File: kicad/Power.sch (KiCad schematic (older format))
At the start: 10 parts

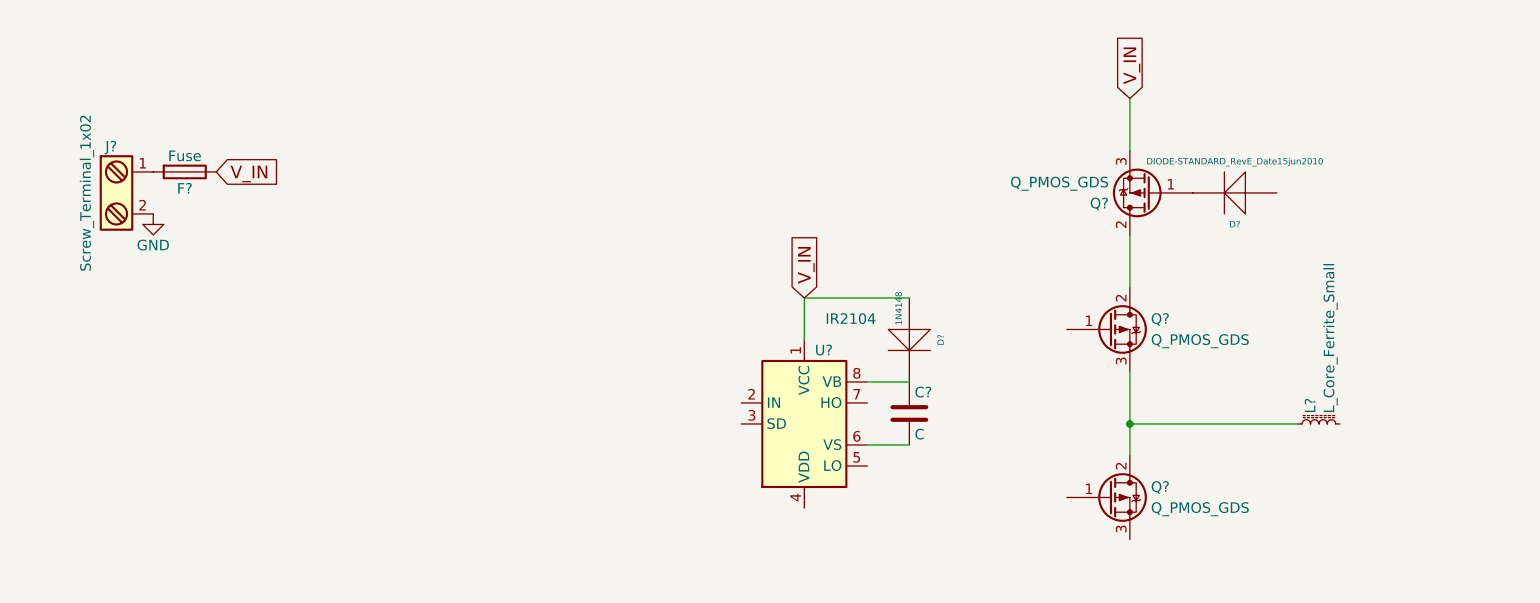
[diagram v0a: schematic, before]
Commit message: Schematical hierarchical structure enhanced
Work on schematical page KiCad
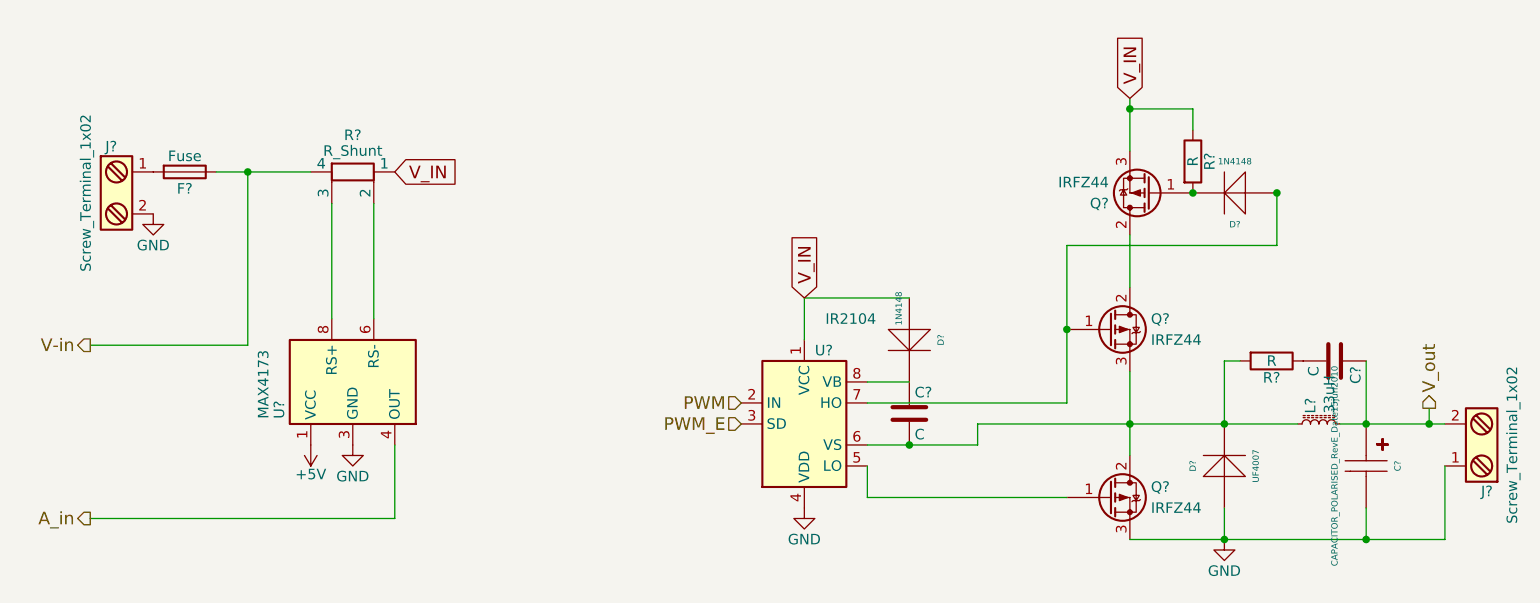
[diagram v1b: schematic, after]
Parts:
- added C?: C, symbol C
- added C?: CAPACITOR_POLARISED_RevE_Date15jun2010, symbol CAPACITOR_POLARISED_RevE_Date15jun2010
- added D?: UF4007, symbol DIODE-STANDARD_RevE_Date15jun2010
- added J?: Screw_Terminal_1x02, symbol Screw_Terminal_1x02
- added R?: R_Shunt, symbol R_Shunt
- added R? (x2): R, symbol R
- added U?: MAX4173, SOIC-8, symbol MAX4173
- D?: value DIODE-STANDARD_RevE_Date15jun2010 -> 1N4148
- L?: value L_Core_Ferrite_Small -> 33uH
- Q? (x3): value Q_PMOS_GDS -> IRFZ44
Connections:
- net GND: now also Q?.3 (S), U?.4 (VDD), C?.2, D?.1 (A), J?.1, U?.3 (GND)
- net V_IN: now also R?.1, R?.1; no longer F?.1
- net at D?.2 (K), Q?.1 (G): now also R?.2
- net at Q?.1 (G): now also D?.1 (A), U?.7 (HO)
- net at L?.1, Q?.2 (D), Q?.3 (S): now also C?.2, U?.6 (VS), D?.2 (K), R?.2
- net at Q?.1 (G): now also U?.5 (LO)
- net PWM: now reaches U?.2 (IN)
- net PWM_E: now reaches U?.3 (SD)
- net V_out: now reaches L?.2
- net V_out: now also C?.1, C?.1, J?.2
- new net: R?.2, U?.6 (RS-)
- new net: R?.3, U?.8 (RS+)
- new net: C?.2, R?.1
- new net +5V: U?.1 (VCC)
- new net A_in: U?.4 (OUT)
- new net V-in: F?.1, R?.4
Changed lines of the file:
@@
 	1    0    0    -1
 $EndComp
-Text GLabel 2150 2050 2    60   Input ~ 0
+Text GLabel 3000 2050 2    60   Input ~ 0
 V_IN
 $Comp
@@
 P 6600 2150
 F 0 "Q?" H 6800 2200 50  0000 L CNN
-F 1 "Q_PMOS_GDS" H 6800 2100 50  0000 L CNN
+F 1 "IRFZ44" H 6800 2100 50  0000 L CNN
 F 2 "" H 6800 2250 50  0001 C CNN
 F 3 "" H 6600 2150 50  0001 C CNN
@@
 P 6400 2800
 F 0 "Q?" H 6600 2850 50  0000 L CNN
-F 1 "Q_PMOS_GDS" H 6600 2750 50  0000 L CNN
+F 1 "IRFZ44" H 6600 2750 50  0000 L CNN
 F 2 "" H 6600 2900 50  0001 C CNN
 F 3 "" H 6400 2800 50  0001 C CNN
@@
 P 6400 3600
 F 0 "Q?" H 6600 3650 50  0000 L CNN
-F 1 "Q_PMOS_GDS" H 6600 3550 50  0000 L CNN
+F 1 "IRFZ44" H 6600 3550 50  0000 L CNN
 F 2 "" H 6600 3700 50  0001 C CNN
 F 3 "" H 6400 3600 50  0001 C CNN
@@
 P 7000 2150
 F 0 "D?" H 7000 2300 30  0000 C CNN
-F 1 "DIODE-STANDARD_RevE_Date15jun2010" H 7000 2000 30  0000 C CNN
+F 1 "1N4148" H 7000 2000 30  0000 C CNN
 F 2 "" H 7000 2150 60  0001 C CNN
 F 3 "" H 7000 2150 60  0001 C CNN
@@
 P 7400 3250
 F 0 "L?" H 7450 3290 50  0000 L CNN
-F 1 "L_Core_Ferrite_Small" H 7450 3200 50  0000 L CNN
+F 1 "33uH" H 7450 3200 50  0000 L CNN
 F 2 "" H 7400 3250 50  0001 C CNN
 F 3 "" H 7400 3250 50  0001 C CNN
@@
 $EndComp
 Wire Wire Line
-	6500 1950 6500 1700
+	6500 1700 6500 1950
 Wire Wire Line
 	6500 2600 6500 2350
 Wire Wire Line
-	6500 3400 6500 3000
-Wire Wire Line
-	7300 3250 6500 3250
+	6500 3000 6500 3400
+Wire Wire Line
+	5775 3250 7300 3250
 Connection ~ 6500 3250
 Text GLabel 4950 2650 1    60   Input ~ 0
@@
 $EndComp
 Wire Wire Line
-	5450 3350 5250 3350
+	5250 3350 5775 3350
+$Comp
+L R_Shunt R?
+U 1 1 5B82012D
+P 2800 2050
+F 0 "R?" V 2625 2050 50  0000 C CNN
+F 1 "R_Shunt" V 2700 2050 50  0000 C CNN
+F 2 "" V 2730 2050 50  0001 C CNN
+F 3 "" H 2800 2050 50  0001 C CNN
+	1    2800 2050
+	0    1    1    0
+$EndComp
+Wire Wire Line
+	2150 2050 2600 2050
+$Comp
+L MAX4173 U?
+U 1 1 5B820270
+P 2800 3050
+F 0 "U?" H 2625 3400 50  0000 L CNN
+F 1 "MAX4173" H 2625 3475 50  0000 L CNN
+F 2 "SOIC-8" H 2800 2700 50  0001 C CIN
+F 3 "" H 2800 3050 50  0001 C CNN
+	1    2800 3050
+	0    -1   -1   0
+$EndComp
+Wire Wire Line
+	2700 2750 2700 2200
+Wire Wire Line
+	2900 2750 2900 2200
+Wire Wire Line
+	2300 2050 2300 2875
+Wire Wire Line
+	2300 2875 1550 2875
+Connection ~ 2300 2050
+Text HLabel 1550 2875 0    60   Output ~ 0
+V-in
+Wire Wire Line
+	3000 3700 1550 3700
+Wire Wire Line
+	3000 3350 3000 3700
+Text HLabel 1550 3700 0    60   Output ~ 0
+A_in
+$Comp
+L +5V #PWR?
+U 1 1 5B82066B
+P 2600 3350
+F 0 "#PWR?" H 2600 3200 50  0001 C CNN
+F 1 "+5V" H 2600 3490 50  0000 C CNN
+F 2 "" H 2600 3350 50  0001 C CNN
+F 3 "" H 2600 3350 50  0001 C CNN
+	1    2600 3350
+	-1   0    0    1
+$EndComp
+$Comp
+L GND #PWR?
+U 1 1 5B8206A3
+P 2800 3350
+F 0 "#PWR?" H 2800 3100 50  0001 C CNN
+F 1 "GND" H 2800 3200 50  0000 C CNN
+F 2 "" H 2800 3350 50  0001 C CNN
+F 3 "" H 2800 3350 50  0001 C CNN
+	1    2800 3350
+	1    0    0    -1
+$EndComp
+Text HLabel 4650 3150 0    60   Input ~ 0
+PWM
+Text HLabel 4650 3250 0    60   Input ~ 0
+PWM_E
+Wire Wire Line
+	5775 3350 5775 3250
+Connection ~ 5450 3350
+Wire Wire Line
+	6200 3150 5250 3150
+Wire Wire Line
+	6200 2400 6200 3150
+Wire Wire Line
+	6200 2400 7200 2400
+Wire Wire Line
+	7200 2400 7200 2150
+Connection ~ 6200 2800
+$Comp
+L R R?
+U 1 1 5B83631E
+P 6800 2000
+F 0 "R?" V 6880 2000 50  0000 C CNN
+F 1 "R" V 6800 2000 50  0000 C CNN
+F 2 "" V 6730 2000 50  0001 C CNN
+F 3 "" H 6800 2000 50  0001 C CNN
+	1    6800 2000
+	1    0    0    -1
+$EndComp
+Connection ~ 6800 2150
+Connection ~ 7200 2150
+Wire Wire Line
+	6800 1850 6800 1750
+Wire Wire Line
+	6800 1750 6500 1750
+Connection ~ 6500 1750
+Wire Wire Line
+	6200 3600 5250 3600
+Wire Wire Line
+	5250 3600 5250 3450
+$Comp
+L GND #PWR?
+U 1 1 5B83651E
+P 4950 3650
+F 0 "#PWR?" H 4950 3400 50  0001 C CNN
+F 1 "GND" H 4950 3500 50  0000 C CNN
+F 2 "" H 4950 3650 50  0001 C CNN
+F 3 "" H 4950 3650 50  0001 C CNN
+	1    4950 3650
+	1    0    0    -1
+$EndComp
+$Comp
+L GND #PWR?
+U 1 1 5B83654C
+P 6950 3800
+F 0 "#PWR?" H 6950 3550 50  0001 C CNN
+F 1 "GND" H 6950 3650 50  0000 C CNN
+F 2 "" H 6950 3800 50  0001 C CNN
+F 3 "" H 6950 3800 50  0001 C CNN
+	1    6950 3800
+	1    0    0    -1
+$EndComp
+$Comp
+L DIODE-STANDARD_RevE_Date15jun2010 D?
+U 1 1 5B83657A
+P 6950 3450
+F 0 "D?" H 6950 3600 30  0000 C CNN
+F 1 "UF4007" H 6950 3300 30  0000 C CNN
+F 2 "" H 6950 3450 60  0001 C CNN
+F 3 "" H 6950 3450 60  0001 C CNN
+	1    6950 3450
+	0    -1   -1   0
+$EndComp
+Wire Wire Line
+	6500 3800 8000 3800
+Wire Wire Line
+	6950 3800 6950 3650
+Connection ~ 6950 3250
+$Comp
+L R R?
+U 1 1 5B836C21
+P 7175 2950
+F 0 "R?" V 7255 2950 50  0000 C CNN
+F 1 "R" V 7175 2950 50  0000 C CNN
+F 2 "" V 7105 2950 50  0001 C CNN
+F 3 "" H 7175 2950 50  0001 C CNN
+	1    7175 2950
+	0    1    1    0
+$EndComp
+$Comp
+L C C?
+U 1 1 5B836C7C
+P 7475 2950
+F 0 "C?" H 7500 3050 50  0000 L CNN
+F 1 "C" H 7500 2850 50  0000 L CNN
+F 2 "" H 7513 2800 50  0001 C CNN
+F 3 "" H 7475 2950 50  0001 C CNN
+	1    7475 2950
+	0    1    1    0
+$EndComp
+Wire Wire Line
+	7025 2950 6950 2950
+Wire Wire Line
+	6950 2950 6950 3250
+Wire Wire Line
+	7500 3250 8000 3250
+Wire Wire Line
+	7625 2950 7625 3250
+Connection ~ 7625 3250
+$Comp
+L CAPACITOR_POLARISED_RevE_Date15jun2010 C?
+U 1 1 5B836DDB
+P 7625 3450
+F 0 "C?" H 7625 3600 30  0000 C CNN
+F 1 "CAPACITOR_POLARISED_RevE_Date15jun2010" H 7625 3300 30  0000 C CNN
+F 2 "" H 7625 3450 60  0001 C CNN
+F 3 "" H 7625 3450 60  0001 C CNN
+	1    7625 3450
+	0    1    1    0
+$EndComp
+Wire Wire Line
+	7625 3800 7625 3650
+Connection ~ 6950 3800
+Wire Wire Line
+	8000 3800 8000 3450
+Connection ~ 7625 3800
+$Comp
+L Screw_Terminal_1x02 J?
+U 1 1 5B836F93
+P 8200 3350
+F 0 "J?" H 8200 3600 50  0000 C TNN
+F 1 "Screw_Terminal_1x02" V 8050 3350 50  0000 C TNN
+F 2 "" H 8200 3125 50  0001 C CNN
+F 3 "" H 8175 3350 50  0001 C CNN
+	1    8200 3350
+	-1   0    0    1
+$EndComp
+Text HLabel 7925 3175 1    60   Output ~ 0
+V_out
+Wire Wire Line
+	7925 3175 7925 3250
+Connection ~ 7925 3250
 $EndSCHEMATC
